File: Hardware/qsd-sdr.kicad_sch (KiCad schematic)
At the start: 42 parts, among them J11 SDR ANT, J12 SDR Out, U7 PI5C3253CQEX, U8 OPA1612AxD

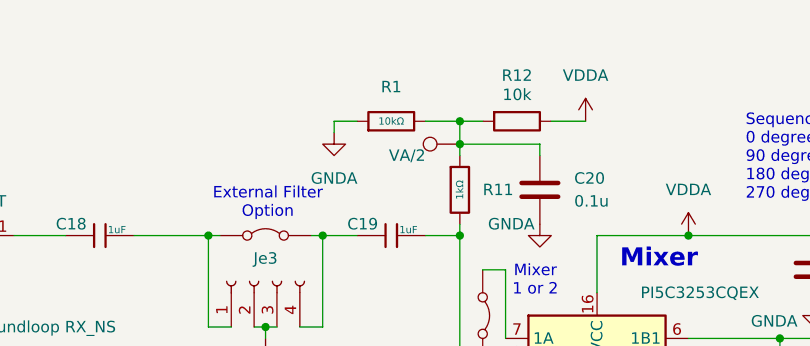
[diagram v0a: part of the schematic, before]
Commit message: Hardware errors found.
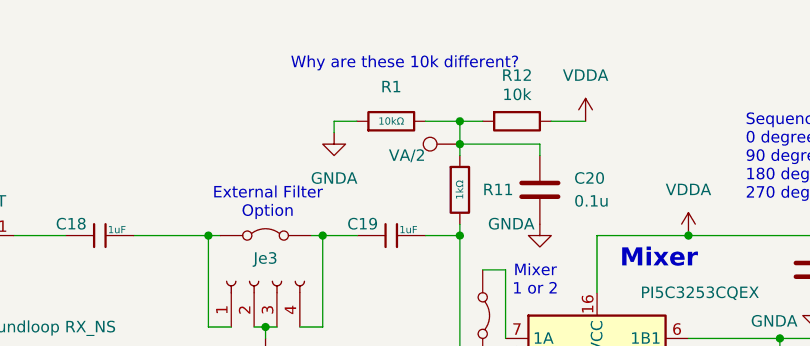
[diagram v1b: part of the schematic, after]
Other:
- note added: "Why are these 10k different?"
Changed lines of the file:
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@@
 		(comment 1 "Rob Frohne")
+	)
+	(text "Why are these 10k different?"
+		(exclude_from_sim no)
+		(at 87.884 39.37 0)
+		(effects
+			(font
+				(size 1.27 1.27)
+			)
+		)
 	)
 	(text "Sequence of clocks:  Q_CLK, I_CLK\n0 degrees:   1,1\n90 degrees:  1,0\n180 degrees: 0,0\n270 degrees: 0,1"
